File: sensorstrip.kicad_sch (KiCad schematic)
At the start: 18 parts, among them J1 USB_C_Receptacle_PowerOnly, SW1 SW_DPDT_x2

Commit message: Update to v3
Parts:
- removed D1, D10, D5, D6, D7, D8, D9: LED, sensorstrip:LED_THT-1.27mm-OrthogonalSMDMount, symbol Device:LED
- removed R2, R3: 220R, Resistor_SMD:R_0603_1608Metric_Pad0.98x0.95mm_HandSolder, symbol Device:R
- removed R4: 120R, Resistor_SMD:R_0603_1608Metric_Pad0.98x0.95mm_HandSolder, symbol Device:R
- added J2: Conn_01x02, Connector_JST:JST_GH_SM02B-GHS-TB_1x02-1MP_P1.25mm_Horizontal, symbol Connector_Generic:Conn_01x02
- added JP1: SolderJumper_2_Open, Jumper:SolderJumper-2_P1.3mm_Open_Pad1.0x1.5mm, symbol Jumper:SolderJumper_2_Open
- renumbered R5 to R2, R6 to R3
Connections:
- net GND: now also J2.2 (Pin_2)
- net VBUS: now also JP1.2 (B)
- net +5V renamed Power_postSwitch
- net Power_postSwitch: now also R1.2, J2.1 (Pin_1), JP1.1 (A); no longer R1.1
- net LEDs-R-Inner renamed LEDs
- net LEDs: now also R1.1; no longer R1.2
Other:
- moved on the sheet: D2, D3, D4, R1

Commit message: Minor tweaks
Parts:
- renumbered D2 to D1, D3 to D2, D4 to D3
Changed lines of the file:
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@@
   (symbol (lib_id "Device:LED") (at 92.456 98.552 0) (unit 1)
     (in_bom yes) (on_board yes)
-    (property "Reference" "D4" (id 0) (at 88.646 101.9718 0)
+    (property "Reference" "D3" (id 0) (at 88.646 101.9718 0)
       (effects (font (size 1.27 1.27)) (justify right))
     )
@@
   (symbol (lib_id "Device:LED") (at 92.71 91.44 0) (unit 1)
     (in_bom yes) (on_board yes)
-    (property "Reference" "D3" (id 0) (at 88.9 94.8598 0)
+    (property "Reference" "D2" (id 0) (at 88.9 94.8598 0)
       (effects (font (size 1.27 1.27)) (justify right))
     )
@@
   (symbol (lib_id "Device:LED") (at 92.71 83.058 0) (unit 1)
     (in_bom yes) (on_board yes)
-    (property "Reference" "D2" (id 0) (at 89.408 87.4394 0)
+    (property "Reference" "D1" (id 0) (at 89.408 87.4394 0)
       (effects (font (size 1.27 1.27)) (justify right))
     )
@@
     )
     (path "/cb16ca99-563a-4e3e-999e-31e3640245a2"
+      (reference "D1") (unit 1) (value "LED") (footprint "sensorstrip:LED_THT-1.27mm-OrthogonalSMDMount")
+    )
+    (path "/63064b45-8333-4184-9fef-8aa5647d0b0b"
       (reference "D2") (unit 1) (value "LED") (footprint "sensorstrip:LED_THT-1.27mm-OrthogonalSMDMount")
     )
-    (path "/63064b45-8333-4184-9fef-8aa5647d0b0b"
+    (path "/0ddf7455-9149-4dbc-979b-f086dbd57a6e"
       (reference "D3") (unit 1) (value "LED") (footprint "sensorstrip:LED_THT-1.27mm-OrthogonalSMDMount")
     )
-    (path "/0ddf7455-9149-4dbc-979b-f086dbd57a6e"
-      (reference "D4") (unit 1) (value "LED") (footprint "sensorstrip:LED_THT-1.27mm-OrthogonalSMDMount")
-    )
     (path "/afd52f1f-8d14-45fe-8984-08ddf10bb430"

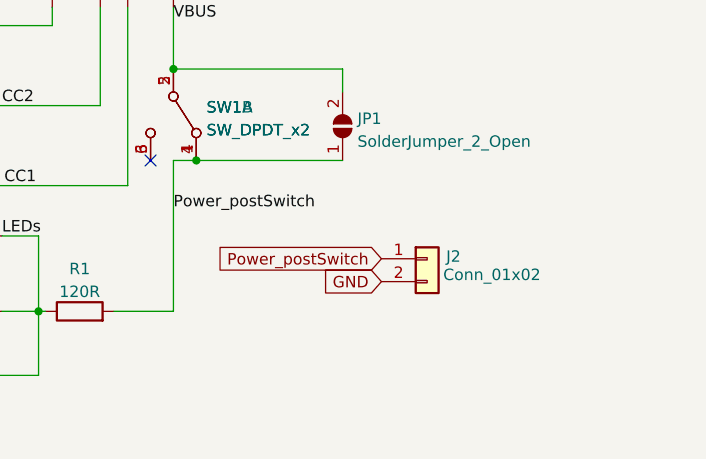
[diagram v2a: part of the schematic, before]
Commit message: Use more appropriate J2 symbol to prevent DRC warning
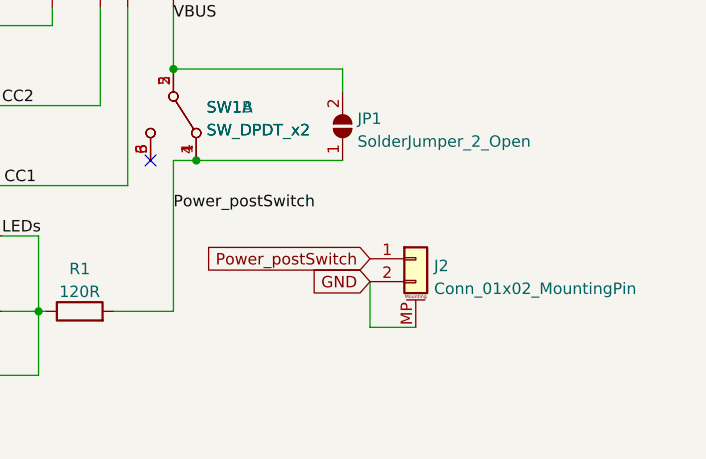
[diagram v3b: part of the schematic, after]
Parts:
- removed J2: Conn_01x02, Connector_JST:JST_GH_SM02B-GHS-TB_1x02-1MP_P1.25mm_Horizontal, symbol Connector_Generic:Conn_01x02
- added J2: Conn_01x02_MountingPin, Connector_JST:JST_GH_SM02B-GHS-TB_1x02-1MP_P1.25mm_Horizontal, symbol Connector_Generic_MountingPin:Conn_01x02_MountingPin
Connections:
- net GND: now also J2.2 (Pin_2), J2.MP (MountPin)
- net Power_postSwitch: now also J2.1 (Pin_1)
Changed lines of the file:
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@@
+    (stroke (width 0) (type default) (color 0 0 0 0))
+  )
+  (wire (pts (xy 137.414 93.218) (xy 142.494 93.218))
     (stroke (width 0) (type default) (color 0 0 0 0))
   )
@@
     (stroke (width 0) (type default) (color 0 0 0 0))
   )
+  (wire (pts (xy 137.414 93.218) (xy 137.414 88.138))
+    (stroke (width 0) (type default) (color 0 0 0 0))
+  )
   (wire (pts (xy 115.57 91.44) (xy 108.966 91.44))
     (stroke (width 0) (type default) (color 0 0 0 0))
@@
     (effects (font (size 1.27 1.27)) (justify left bottom))
   )
-  (global_label "Power_postSwitch" (shape input) (at 138.684 85.598 180) (fields_autoplaced)
+  (global_label "Power_postSwitch" (shape input) (at 137.414 85.598 180) (fields_autoplaced)
     (effects (font (size 1.27 1.27)) (justify right))
-    (property "Intersheet References" "${INTERSHEET_REFS}" (id 0) (at 119.519 85.5186 0)
+    (property "Intersheet References" "${INTERSHEET_REFS}" (id 0) (at 118.249 85.5186 0)
       (effects (font (size 1.27 1.27)) (justify right) hide)
     )
   )
-  (global_label "GND" (shape input) (at 138.684 88.138 180) (fields_autoplaced)
+  (global_label "GND" (shape input) (at 137.414 88.138 180) (fields_autoplaced)
     (effects (font (size 1.27 1.27)) (justify right))
-    (property "Intersheet References" "${INTERSHEET_REFS}" (id 0) (at 132.4004 88.0586 0)
+    (property "Intersheet References" "${INTERSHEET_REFS}" (id 0) (at 131.1304 88.0586 0)
       (effects (font (size 1.27 1.27)) (justify right) hide)
     )
@@
     (pin "2")
   )
-  (symbol (lib_id "Connector_Generic:Conn_01x02") (at 143.764 85.598 0) (unit 1)
-    (in_bom yes) (on_board yes)
-    (property "Reference" "J2" (id 0) (at 145.8718 85.344 0)
-      (effects (font (size 1.27 1.27)) (justify left))
-    )
-    (property "Value" "Conn_01x02" (id 1) (at 145.542 87.376 0)
-      (effects (font (size 1.27 1.27)) (justify left))
-    )
-    (property "Footprint" "Connector_JST:JST_GH_SM02B-GHS-TB_1x02-1MP_P1.25mm_Horizontal" (id 2) (at 143.764 85.598 0)
-      (effects (font (size 1.27 1.27)) hide)
-    )
-    (property "Datasheet" "~" (id 3) (at 143.764 85.598 0)
-      (effects (font (size 1.27 1.27)) hide)
-    )
-    (pin "1")
-    (pin "2")
+  (symbol (lib_id "Connector_Generic_MountingPin:Conn_01x02_MountingPin") (at 142.494 85.598 0) (unit 1)
+    (in_bom yes) (on_board yes) (fields_autoplaced)
+    (property "Reference" "J2" (id 0) (at 144.526 86.3889 0)
+      (effects (font (size 1.27 1.27)) (justify left))
+    )
+    (property "Value" "Conn_01x02_MountingPin" (id 1) (at 144.526 88.9258 0)
+      (effects (font (size 1.27 1.27)) (justify left))
+    )
+    (property "Footprint" "Connector_JST:JST_GH_SM02B-GHS-TB_1x02-1MP_P1.25mm_Horizontal" (id 2) (at 142.494 85.598 0)
+      (effects (font (size 1.27 1.27)) hide)
+    )
+    (property "Datasheet" "~" (id 3) (at 142.494 85.598 0)
+      (effects (font (size 1.27 1.27)) hide)
+    )
+    (pin "1")
+    (pin "2")
+    (pin "MP")
   )
   (symbol (lib_id "Device:R") (at 85.598 68.58 90) (unit 1)
@@
       (reference "J1") (unit 1) (value "USB_C_Receptacle_PowerOnly") (footprint "sensorstrip:DEALON USB Type-C 6Pin")
     )
-    (path "/349e0a2e-ef26-44b1-9b2a-56b14c45a6f3"
-      (reference "J2") (unit 1) (value "Conn_01x02") (footprint "Connector_JST:JST_GH_SM02B-GHS-TB_1x02-1MP_P1.25mm_Horizontal")
+    (path "/315ff913-0563-42e8-b327-2a3d53427536"
+      (reference "J2") (unit 1) (value "Conn_01x02_MountingPin") (footprint "Connector_JST:JST_GH_SM02B-GHS-TB_1x02-1MP_P1.25mm_Horizontal")
     )
     (path "/5067f85e-27a3-4223-b92d-c31e4e482a17"
